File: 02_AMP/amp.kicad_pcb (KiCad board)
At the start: 2 copper layers, 23 parts, among them J1 Screw_Terminal_01x03, J2 Screw_Terminal_01x02, J3 Screw_Terminal_01x02, U1 LM1875

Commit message: 基板外形仮設定 #3
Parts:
- added REF**: MountingHole_3.2mm_M3, MountingHole:MountingHole_3.2mm_M3, F.Cu at (146.8, 79.4)
- added REF**: MountingHole_3.2mm_M3, MountingHole:MountingHole_3.2mm_M3, F.Cu at (202.7, 125.7)
- added REF**: MountingHole_3.2mm_M3, MountingHole:MountingHole_3.2mm_M3, F.Cu at (202.7, 79.4)
- added REF**: MountingHole_3.2mm_M3, MountingHole:MountingHole_3.2mm_M3, F.Cu at (146.8, 125.7)
- moved J1 6.48 mm to (148.2, 108.5)
- moved J3 4.06 mm to (148.2, 95.2)
- moved TP2 3.38 mm to (165.5, 110.5)
- moved TP5 3.35 mm to (159.0, 121.5)
- moved TP1 2.73 mm to (153.9, 90.9)
- moved TP6 0.68 mm to (153.2, 78.9)
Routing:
- net -30V: track 40.5 -> 43.2 mm
- net +30V: track 48.8 -> 46.1 mm
- net Vin_AC: track 22.5 -> 23.5 mm
- net Vin: track 24.2 -> 24.8 mm
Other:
- board outline added: 63 x 53.5 mm
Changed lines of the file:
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@@
   )
   (footprint "TestPoint:TestPoint_THTPad_D2.5mm_Drill1.2mm" (layer "F.Cu")
-    (at 167.386 107.696)
+    (at 165.481 110.49)
     (descr "THT pad as test Point, diameter 2.5mm, hole diameter 1.2mm ")
     (tags "test point THT pad")
@@
   )
   (footprint "TestPoint:TestPoint_THTPad_D2.5mm_Drill1.2mm" (layer "F.Cu")
-    (at 152.908 78.232)
+    (at 153.162 78.867)
     (descr "THT pad as test Point, diameter 2.5mm, hole diameter 1.2mm ")
     (tags "test point THT pad")
@@
   )
   (footprint "TerminalBlock:TerminalBlock_bornier-2_P5.08mm" (layer "F.Cu")
-    (at 148.209 99.314 -90)
+    (at 148.209 95.25 -90)
     (descr "simple 2-pin terminal block, pitch 5.08mm, revamped version of bornier2")
     (tags "terminal block bornier2")
@@
   )
   (footprint "TerminalBlock:TerminalBlock_bornier-3_P5.08mm" (layer "F.Cu")
-    (at 148.209 114.935 -90)
+    (at 148.209 108.458 -90)
     (descr "simple 3-pin terminal block, pitch 5.08mm, revamped version of bornier3")
     (tags "terminal block bornier3")
@@
     )
   )
+  (footprint "MountingHole:MountingHole_3.2mm_M3" (layer "F.Cu")
+    (at 146.812 79.375)
+    (descr "Mounting Hole 3.2mm, no annular, M3")
+    (tags "mounting hole 3.2mm no annular m3")
+    (attr exclude_from_pos_files exclude_from_bom)
+    (fp_text reference "REF**" (at 0 -4.2) (layer "F.SilkS") hide
+        (effects (font (size 1 1) (thickness 0.15)))
+    )
+    (fp_text value "MountingHole_3.2mm_M3" (at 0 4.2) (layer "F.Fab") hide
+        (effects (font (size 1 1) (thickness 0.15)))
+    )
+    (fp_circle (center 0 0) (end 3.2 0)
+      (stroke (width 0.15) (type solid)) (fill none) (layer "Cmts.User"))
+    (fp_circle (center 0 0) (end 3.45 0)
+      (stroke (width 0.05) (type solid)) (fill none) (layer "F.CrtYd"))
+    (pad "" np_thru_hole circle (at 0 0) (size 3.2 3.2) (drill 3.2) (layers "*.Cu" "*.Mask"))
+  )
   (footprint "Capacitor_SMD:C_0603_1608Metric" (layer "F.Cu")
     (at 176.53 100.203 180)
@@
       (rotate (xyz 0 0 0))
     )
+  )
+  (footprint "MountingHole:MountingHole_3.2mm_M3" (layer "F.Cu")
+    (at 202.692 125.73)
+    (descr "Mounting Hole 3.2mm, no annular, M3")
+    (tags "mounting hole 3.2mm no annular m3")
+    (attr exclude_from_pos_files exclude_from_bom)
+    (fp_text reference "REF**" (at 0 -4.2) (layer "F.SilkS") hide
+        (effects (font (size 1 1) (thickness 0.15)))
+    )
+    (fp_text value "MountingHole_3.2mm_M3" (at 0 4.2) (layer "F.Fab") hide
+        (effects (font (size 1 1) (thickness 0.15)))
+    )
+    (fp_circle (center 0 0) (end 3.2 0)
+      (stroke (width 0.15) (type solid)) (fill none) (layer "Cmts.User"))
+    (fp_circle (center 0 0) (end 3.45 0)
+      (stroke (width 0.05) (type solid)) (fill none) (layer "F.CrtYd"))
+    (pad "" np_thru_hole circle (at 0 0) (size 3.2 3.2) (drill 3.2) (layers "F&B.Cu" "*.Mask"))
+  )
+  (footprint "MountingHole:MountingHole_3.2mm_M3" (layer "F.Cu")
+    (at 202.692 79.375)
+    (descr "Mounting Hole 3.2mm, no annular, M3")
+    (tags "mounting hole 3.2mm no annular m3")
+    (attr exclude_from_pos_files exclude_from_bom)
+    (fp_text reference "REF**" (at 0 -4.2) (layer "F.SilkS") hide
+        (effects (font (size 1 1) (thickness 0.15)))
+    )
+    (fp_text value "MountingHole_3.2mm_M3" (at 0 4.2) (layer "F.Fab") hide
+        (effects (font (size 1 1) (thickness 0.15)))
+    )
+    (fp_circle (center 0 0) (end 3.2 0)
+      (stroke (width 0.15) (type solid)) (fill none) (layer "Cmts.User"))
+    (fp_circle (center 0 0) (end 3.45 0)
+      (stroke (width 0.05) (type solid)) (fill none) (layer "F.CrtYd"))
+    (pad "" np_thru_hole circle (at 0 0) (size 3.2 3.2) (drill 3.2) (layers "F&B.Cu" "*.Mask"))
   )
   (footprint "TestPoint:TestPoint_THTPad_D2.5mm_Drill1.2mm" (layer "F.Cu")
@@
   )
   (footprint "TestPoint:TestPoint_THTPad_D2.5mm_Drill1.2mm" (layer "F.Cu")
-    (at 152.654 93.345)
+    (at 153.924 90.932)
     (descr "THT pad as test Point, diameter 2.5mm, hole diameter 1.2mm ")
     (tags "test point THT pad")
@@
   )
   (footprint "TestPoint:TestPoint_THTPad_D2.5mm_Drill1.2mm" (layer "F.Cu")
-    (at 156.972 118.872)
+    (at 159.004 121.539)
     (descr "THT pad as test Point, diameter 2.5mm, hole diameter 1.2mm ")
     (tags "test point THT pad")
@@
       (rotate (xyz 0 0 0))
     )
+  )
+  (footprint "MountingHole:MountingHole_3.2mm_M3" (layer "F.Cu")
+    (at 146.812 125.73)
+    (descr "Mounting Hole 3.2mm, no annular, M3")
+    (tags "mounting hole 3.2mm no annular m3")
+    (attr exclude_from_pos_files exclude_from_bom)
+    (fp_text reference "REF**" (at 0 -4.2) (layer "F.SilkS") hide
+        (effects (font (size 1 1) (thickness 0.15)))
+    )
+    (fp_text value "MountingHole_3.2mm_M3" (at 0 4.2) (layer "F.Fab") hide
+        (effects (font (size 1 1) (thickness 0.15)))
+    )
+    (fp_circle (center 0 0) (end 3.2 0)
+      (stroke (width 0.15) (type solid)) (fill none) (layer "Cmts.User"))
+    (fp_circle (center 0 0) (end 3.45 0)
+      (stroke (width 0.05) (type solid)) (fill none) (layer "F.CrtYd"))
+    (pad "" np_thru_hole circle (at 0 0) (size 3.2 3.2) (drill 3.2) (layers "F&B.Cu" "*.Mask"))
   )
   (footprint "Capacitor_THT:CP_Radial_Tantal_D6.0mm_P2.50mm" (layer "F.Cu")
@@
     )
   )
-  (segment (start 152.654 99.949) (end 152.654 93.345) (width 0.5) (layer "F.Cu") (net 1))
+  (gr_line (start 202.692 129.286) (end 146.812 129.286)
+    (stroke (width 0.1) (type default)) (layer "Edge.Cuts"))
+  (gr_line (start 146.812 75.819) (end 202.692 75.819)
+    (stroke (width 0.1) (type default)) (layer "Edge.Cuts"))
+  (gr_line (start 143.256 79.375) (end 143.256 125.73)
+    (stroke (width 0.1) (type default)) (layer "Edge.Cuts"))
+  (gr_arc (start 202.692 75.819) (mid 205.206472 76.860528) (end 206.248 79.375)
+    (stroke (width 0.1) (type default)) (layer "Edge.Cuts"))
+  (gr_arc (start 206.248 125.73) (mid 205.206472 128.244472) (end 202.692 129.286)
+    (stroke (width 0.1) (type default)) (layer "Edge.Cuts"))
+  (gr_line (start 206.248 79.375) (end 206.248 125.73)
+    (stroke (width 0.1) (type default)) (layer "Edge.Cuts"))
+  (gr_arc (start 143.256 79.375) (mid 144.297528 76.860528) (end 146.812 75.819)
+    (stroke (width 0.1) (type default)) (layer "Edge.Cuts"))
+  (gr_arc (start 146.812 129.286) (mid 144.297528 128.244472) (end 143.256 125.73)
+    (stroke (width 0.1) (type default)) (layer "Edge.Cuts"))
+  (segment (start 156.591 105.22) (end 151.701 100.33) (width 0.5) (layer "F.Cu") (net 1))
+  (segment (start 148.209 100.33) (end 153.924 94.615) (width 0.5) (layer "F.Cu") (net 1))
   (segment (start 158.305 105.22) (end 158.955 104.57) (width 0.5) (layer "F.Cu") (net 1))
-  (segment (start 148.209 104.394) (end 152.654 99.949) (width 0.5) (layer "F.Cu") (net 1))
-  (segment (start 155.765 104.394) (end 156.591 105.22) (width 0.5) (layer "F.Cu") (net 1))
-  (segment (start 148.209 104.394) (end 155.765 104.394) (width 0.5) (layer "F.Cu") (net 1))
+  (segment (start 151.701 100.33) (end 148.209 100.33) (width 0.5) (layer "F.Cu") (net 1))
+  (segment (start 153.924 94.615) (end 153.924 90.932) (width 0.5) (layer "F.Cu") (net 1))
   (segment (start 156.591 105.22) (end 158.305 105.22) (width 0.5) (layer "F.Cu") (net 1))
   (segment (start 181.229 104.59) (end 181.2 104.619) (width 2) (layer "F.Cu") (net 2))
   (segment (start 181.2 97.376) (end 181.229 97.405) (width 2) (layer "F.Cu") (net 2))
   (segment (start 181.229 97.405) (end 181.229 104.59) (width 2) (layer "F.Cu") (net 2))
-  (segment (start 161.036 125.095) (end 181.356 104.775) (width 2) (layer "B.Cu") (net 2))
-  (segment (start 148.209 125.095) (end 161.036 125.095) (width 2) (layer "B.Cu") (net 2))
+  (segment (start 148.209 118.618) (end 167.513 118.618) (width 2) (layer "B.Cu") (net 2))
+  (segment (start 167.513 118.618) (end 181.356 104.775) (width 2) (layer "B.Cu") (net 2))
   (segment (start 177.8 97.376) (end 177.8 102.108) (width 2) (layer "F.Cu") (net 4))
   (segment (start 177.8 102.108) (end 175.133 104.775) (width 2) (layer "F.Cu") (net 4))
-  (segment (start 148.209 114.935) (end 166.473 114.935) (width 2) (layer "B.Cu") (net 4))
+  (segment (start 148.209 108.458) (end 154.686 114.935) (width 2) (layer "B.Cu") (net 4))
+  (segment (start 166.473 114.935) (end 175.133 106.275) (width 2) (layer "B.Cu") (net 4))
+  (segment (start 154.686 114.935) (end 166.473 114.935) (width 2) (layer "B.Cu") (net 4))
   (segment (start 175.133 106.275) (end 175.133 104.775) (width 2) (layer "B.Cu") (net 4))
-  (segment (start 166.473 114.935) (end 175.133 106.275) (width 2) (layer "B.Cu") (net 4))
   (segment (start 173.907625 114.173) (end 176.911 117.176375) (width 0.5) (layer "F.Cu") (net 5))
   (segment (start 173.672 114.173) (end 173.907625 114.173) (width 0.5) (layer "F.Cu") (net 5))
@@
   (segment (start 173.736 112.331) (end 173.672 112.395) (width 0.5) (layer "F.Cu") (net 8))
   (segment (start 178.054 112.331) (end 173.736 112.331) (width 0.5) (layer "F.Cu") (net 8))
-  (segment (start 165.732 107.696) (end 167.386 107.696) (width 0.5) (layer "F.Cu") (net 9))
   (segment (start 160.64 107.52) (end 161.29 106.87) (width 0.5) (layer "F.Cu") (net 9))
   (segment (start 158.955 107.52) (end 160.64 107.52) (width 0.5) (layer "F.Cu") (net 9))
+  (segment (start 165.481 107.445) (end 165.481 110.49) (width 0.5) (layer "F.Cu") (net 9))
   (segment (start 164.906 106.87) (end 174.4 97.376) (width 0.5) (layer "F.Cu") (net 9))
   (segment (start 161.29 106.87) (end 164.906 106.87) (width 0.5) (layer "F.Cu") (net 9))
-  (segment (start 164.906 106.87) (end 165.732 107.696) (width 0.5) (layer "F.Cu") (net 9))
+  (segment (start 164.906 106.87) (end 165.481 107.445) (width 0.5) (layer "F.Cu") (net 9))
 )

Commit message: ベタ面とvia配置
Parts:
- moved R3 2.41 mm to (172.8, 111.8)
- moved R4 2.41 mm to (172.8, 110.0)
- moved C6 2.31 mm to (175.4, 115.4)
- moved R5 1.30 mm to (177.8, 110.2)
- moved TP5 0.63 mm to (158.6, 122.0)
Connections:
- TP5 pad 1: unconnected-(TP5-Pad1) -> GND
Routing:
- net Net-(U1--): track 23.5 -> 21.3 mm
- net Net-(R4-Pad2): track 7.49 -> 8.44 mm
- net GND: vias 0 -> 16
- added copper zone on B.Cu, net GND
- added copper zone on F.Cu, net GND

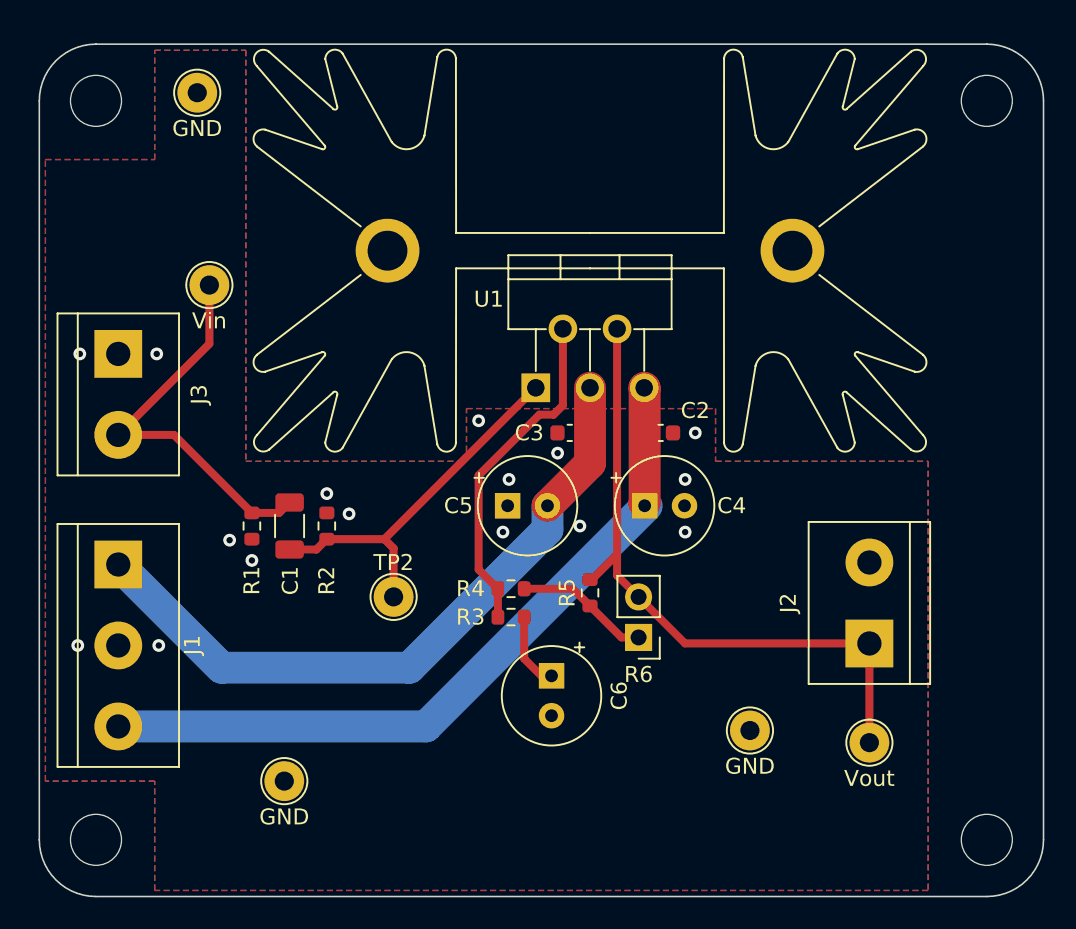
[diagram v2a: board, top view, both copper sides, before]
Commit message: ターミナルのピンアサインシルク
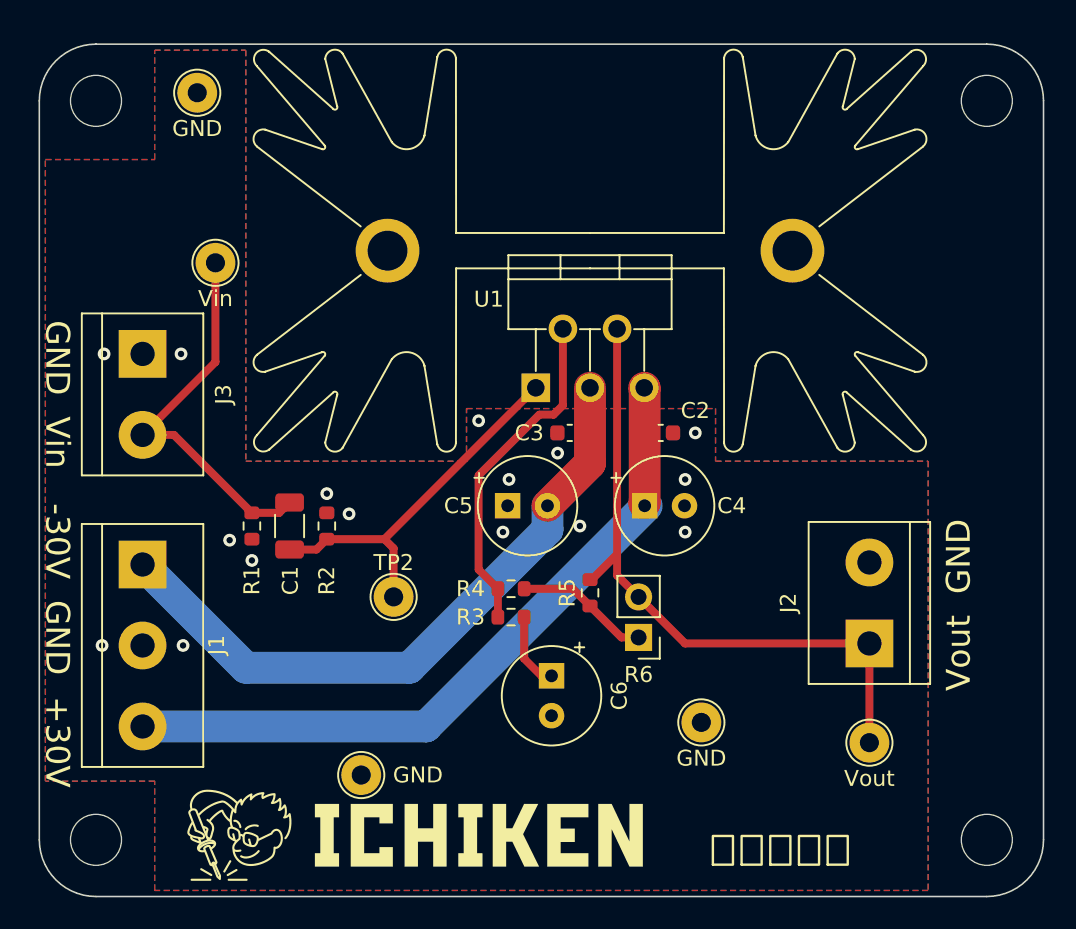
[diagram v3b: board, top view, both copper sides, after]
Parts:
- moved TP5 4.84 mm to (163.4, 121.7)
- moved TP4 3.09 mm to (184.8, 118.4)
- moved J1 1.52 mm to (149.7, 108.5)
- moved J3 1.52 mm to (149.7, 95.2)
- moved TP1 1.45 mm to (154.3, 89.5)
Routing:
- net -30V: track 43.2 -> 41.7 mm
- net +30V: track 46.1 -> 44.6 mm
- net Vin: track 24.8 -> 24.2 mm
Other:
- board text added: "-30V GND +30V"
- board text added: "GND Vin"
- board text added: "Vout GND"
- board text added: "アンプ基板"
